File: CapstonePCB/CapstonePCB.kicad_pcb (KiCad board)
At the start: 2 copper layers, 43 parts, among them J1 Conn_02x40_Counter_Clockwise, J2 Barrel_Jack, J3 512964594, SW1 SW_Push, SW2 SW_Push, SW3 SW_Push, U1 NUCLEO64-F411RE, U2 LP-MSPM0G3507, U3 STSPIN220, U4 SN74AHC14N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

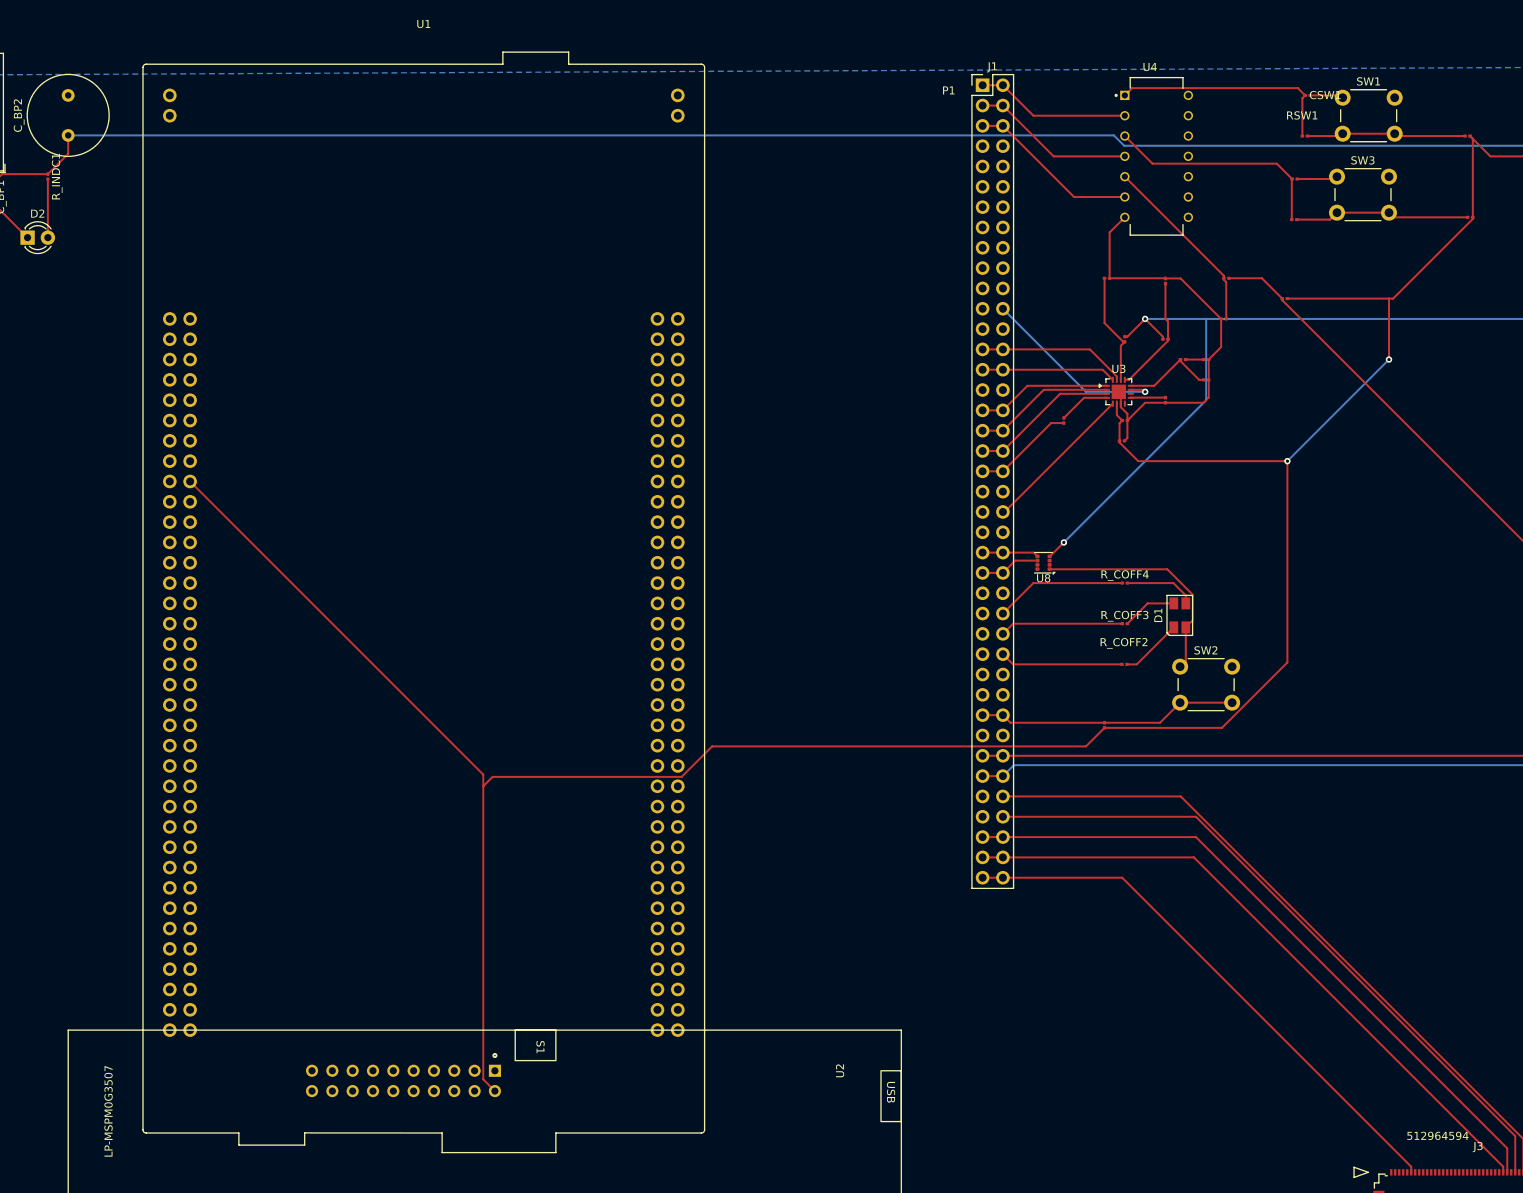
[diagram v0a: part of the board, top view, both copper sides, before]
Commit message: Updated silk-screen
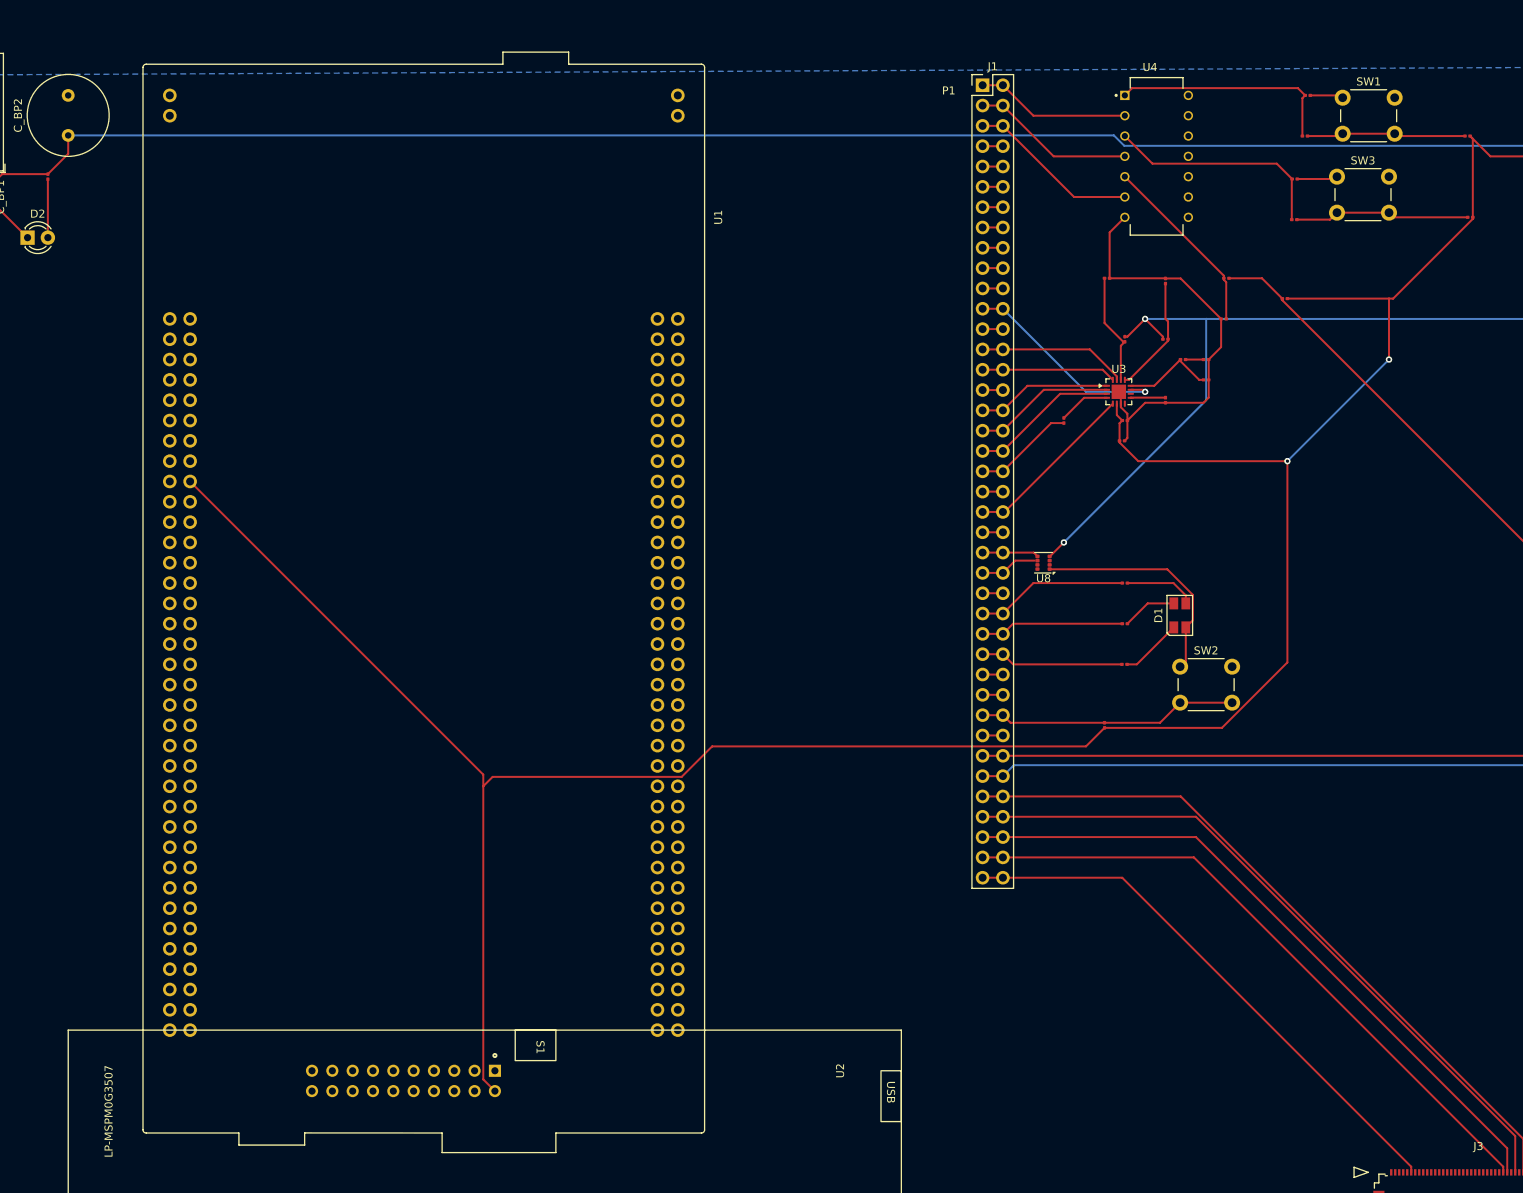
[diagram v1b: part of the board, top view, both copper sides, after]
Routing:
- net Net-(J1-Pin_23): track 24.0 -> 26.5 mm
- net Net-(J1-Pin_57): track 15.4 -> 17.9 mm
- net Net-(J1-Pin_55): track 15.4 -> 18.0 mm
- net Net-(J1-Pin_73): track 85.1 -> 87.7 mm
- net Net-(J1-Pin_71): track 87.0 -> 89.5 mm
- net Net-(J1-Pin_7): track 0.00 -> 2.54 mm
- net Net-(J1-Pin_65): track 0.00 -> 2.54 mm
- net Net-(J1-Pin_61): track 0.00 -> 2.54 mm
- net Net-(J1-Pin_59): track 0.00 -> 2.54 mm
- net Net-(J1-Pin_53): track 16.5 -> 19.0 mm
- net Net-(J1-Pin_51): track 0.00 -> 2.54 mm
- net Net-(J1-Pin_45): track 0.00 -> 2.54 mm
- net Net-(J1-Pin_43): track 19.3 -> 21.9 mm
- net Net-(J1-Pin_41): track 0.00 -> 2.54 mm
- net Net-(J1-Pin_31): track 0.00 -> 2.54 mm
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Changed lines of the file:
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@@
 			(at 0 -1.05 0)
 			(layer "F.SilkS")
+			(hide yes)
 			(effects
 				(font
@@
 			(at -0.345 -2.54 0)
 			(layer "F.SilkS")
+			(hide yes)
 			(effects
 				(font
@@
 			(at 0 -1.05 90)
 			(layer "F.SilkS")
+			(hide yes)
 			(effects
 				(font
@@
 			(layer "F.Fab")
 		)
-		(fp_text user "512964594"
-			(at -5.1816 -6.604 0)
-			(layer "F.SilkS")
-			(effects
-				(font
-					(size 1 1)
-					(thickness 0.15)
-				)
-			)
-		)
-		(fp_text user "512964594"
-			(at -5.1816 -6.604 0)
-			(layer "F.Fab")
-			(effects
-				(font
-					(size 1 1)
-					(thickness 0.15)
-				)
-			)
-		)
 		(pad "1" smd rect
 			(at -11 -2.08)
@@
 			(at -0.055 -2.74 0)
 			(layer "F.SilkS")
+			(hide yes)
 			(effects
 				(font
@@
 			(at 0 -1.05 0)
 			(layer "F.SilkS")
+			(hide yes)
 			(effects
 				(font
@@
 		(tags "ST Morpho Connector 144 STLink")
 		(property "Reference" "U1"
-			(at 31.75 -36.83 0)
+			(at 68.58 -12.7 270)
 			(layer "F.SilkS")
 			(effects
@@
 		)
 		(property "Value" "NUCLEO64-F411RE"
-			(at 31.75 -35.56 0)
+			(at 31.75 -17.78 0)
 			(layer "F.Fab")
 			(effects
@@
 			(at -2.22 0 0)
 			(layer "F.SilkS")
+			(hide yes)
 			(effects
 				(font
@@
 	)
 	(segment
+		(start 147.32 29.21)
+		(end 149.86 29.21)
+		(width 0.25)
+		(layer "F.Cu")
+		(net 118)
+	)
+	(segment
+		(start 147.32 54.61)
+		(end 149.86 54.61)
+		(width 0.25)
+		(layer "F.Cu")
+		(net 119)
+	)
+	(segment
+		(start 147.32 36.83)
+		(end 149.86 36.83)
+		(width 0.25)
+		(layer "F.Cu")
+		(net 120)
+	)
+	(segment
 		(start 152.9325 54.0775)
 		(end 149.86 57.15)
@@
 	)
 	(segment
+		(start 147.32 39.37)
+		(end 149.86 39.37)
+		(width 0.25)
+		(layer "F.Cu")
+		(net 123)
+	)
+	(segment
+		(start 147.32 31.75)
+		(end 149.86 31.75)
+		(width 0.25)
+		(layer "F.Cu")
+		(net 124)
+	)
+	(segment
 		(start 162.8625 54.5775)
 		(end 154.9725 54.5775)
@@
 	)
 	(segment
+		(start 147.32 41.91)
+		(end 149.86 41.91)
+		(width 0.25)
+		(layer "F.Cu")
+		(net 127)
+	)
+	(segment
+		(start 147.32 44.45)
+		(end 149.86 44.45)
+		(width 0.25)
+		(layer "F.Cu")
+		(net 128)
+	)
+	(segment
 		(start 167.3825 54.5775)
 		(end 167.64 54.835)
@@
 	)
 	(segment
+		(start 147.32 46.99)
+		(end 149.86 46.99)
+		(width 0.25)
+		(layer "F.Cu")
+		(net 129)
+	)
+	(segment
 		(start 147.32 21.59)
 		(end 149.86 21.59)
@@
 	)
 	(segment
+		(start 147.32 26.67)
+		(end 149.86 26.67)
+		(width 0.25)
+		(layer "F.Cu")
+		(net 131)
+	)
+	(segment
+		(start 147.32 34.29)
+		(end 149.86 34.29)
+		(width 0.25)
+		(layer "F.Cu")
+		(net 132)
+	)
+	(segment
+		(start 147.32 24.13)
+		(end 149.86 24.13)
+		(width 0.25)
+		(layer "F.Cu")
+		(net 133)
+	)
+	(segment
 		(start 160.0025 55.5775)
 		(end 157.48 58.1)
@@
 	)
 	(segment
-		(start 169.5 96.2)
-		(end 172.01 93.69)
+		(start 147.32 95.25)
+		(end 149.86 95.25)
 		(width 0.25)
 		(layer "F.Cu")
@@
 	)
 	(segment
-		(start 147.32 95.25)
-		(end 149.86 95.25)
+		(start 169.5 96.2)
+		(end 172.01 93.69)
 		(width 0.25)
 		(layer "F.Cu")
@@
 	)
 	(segment
+		(start 147.32 72.39)
+		(end 149.86 72.39)
+		(width 0.25)
+		(layer "F.Cu")
+		(net 149)
+	)
+	(segment
+		(start 147.32 90.17)
+		(end 149.86 90.17)
+		(width 0.25)
+		(layer "F.Cu")
+		(net 150)
+	)
+	(segment
 		(start 147.32 102.87)
 		(end 149.86 102.87)
@@
 	)
 	(segment
+		(start 147.32 105.41)
+		(end 149.86 105.41)
+		(width 0.25)
+		(layer "F.Cu")
+		(net 152)
+	)
+	(segment
 		(start 172.08781 105.41)
 		(end 149.86 105.41)
@@
 	)
 	(segment
+		(start 147.32 87.63)
+		(end 149.86 87.63)
+		(width 0.25)
+		(layer "F.Cu")
+		(net 153)
+	)
+	(segment
 		(start 164.735 88.9)
 		(end 151.13 88.9)
@@
 	)
 	(segment
+		(start 147.32 82.55)
+		(end 149.86 82.55)
+		(width 0.25)
+		(layer "F.Cu")
+		(net 154)
+	)
+	(segment
 		(start 153.67 78.74)
 		(end 149.86 82.55)
@@
 	)
 	(segment
+		(start 147.32 80.01)
+		(end 149.86 80.01)
+		(width 0.25)
+		(layer "F.Cu")
+		(net 155)
+	)
+	(segment
 		(start 151.395 75.935)
 		(end 153.82175 75.935)
@@
 	)
 	(segment
+		(start 147.32 107.95)
+		(end 149.86 107.95)
+		(width 0.25)
+		(layer "F.Cu")
+		(net 160)
+	)
+	(segment
 		(start 213.9 152.4)
 		(end 213.9 147.86)
@@
 	)
 	(segment
+		(start 147.32 92.71)
+		(end 149.86 92.71)
+		(width 0.25)
+		(layer "F.Cu")
+		(net 162)
+	)
+	(segment
+		(start 147.32 97.79)
+		(end 149.86 97.79)
+		(width 0.25)
+		(layer "F.Cu")
+		(net 163)
+	)
+	(segment
 		(start 147.32 74.93)
 		(end 149.86 74.93)
@@
 	)
 	(segment
+		(start 147.32 67.31)
+		(end 149.86 67.31)
+		(width 0.25)
+		(layer "F.Cu")
+		(net 165)
+	)
+	(segment
+		(start 147.32 69.85)
+		(end 149.86 69.85)
+		(width 0.25)
+		(layer "F.Cu")
+		(net 166)
+	)
+	(segment
 		(start 163.6 56.315)
 		(end 150.065 69.85)
@@
 		(width 0.25)
 		(layer "F.Cu")
+		(net 167)
+	)
+	(segment
+		(start 147.32 85.09)
+		(end 149.86 85.09)
+		(width 0.25)
+		(layer "F.Cu")

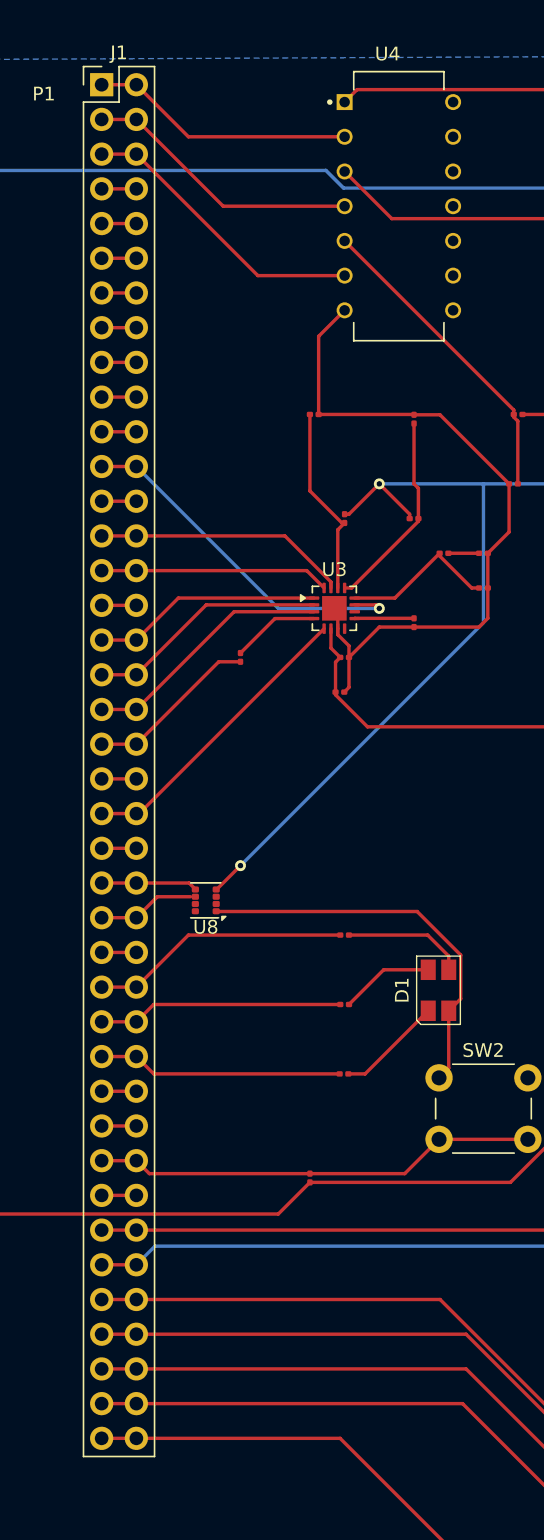
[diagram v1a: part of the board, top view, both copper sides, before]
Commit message: Changed I2C light sensor to different type so pin spacing is not an issue
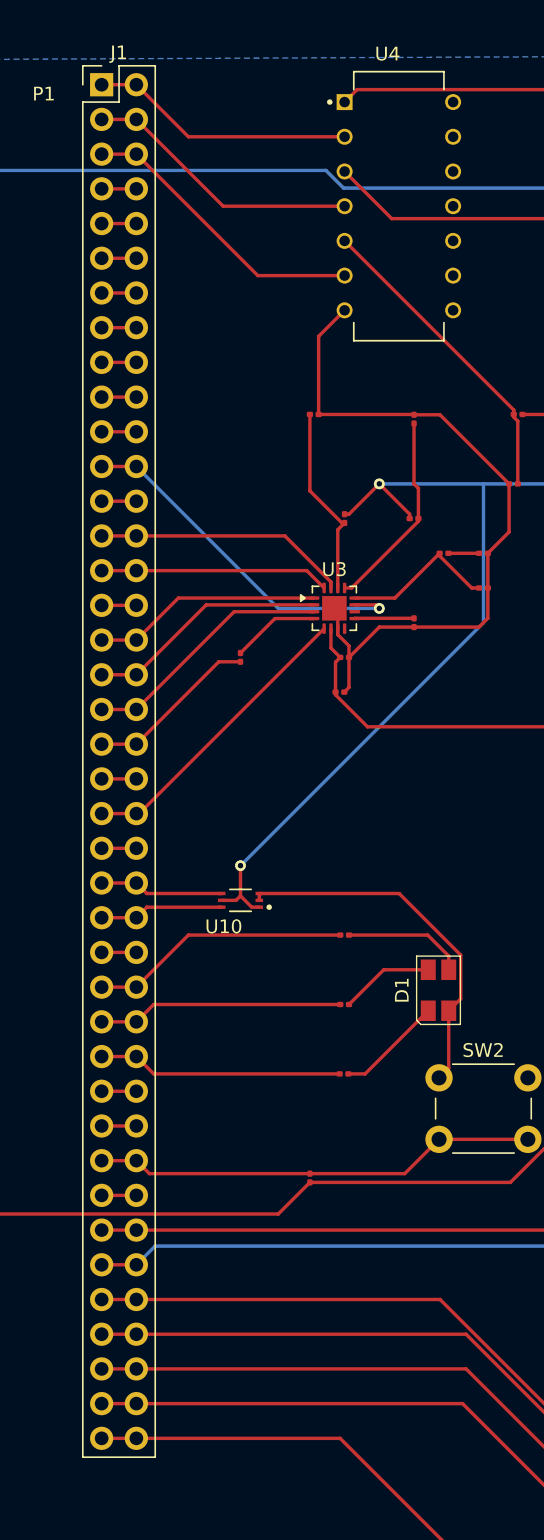
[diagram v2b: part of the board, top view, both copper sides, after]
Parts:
- removed U8: APDS-9306, OptoDevice:Broadcom_LGA-8_2x2mm_P0.53mm
- added U10: BH1750FVI-TR, BH1750FVI-TR:XDCR_BH1750FVI-TR, F.Cu at (157.5, 76.2)
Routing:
- net VDD: track 285.0 -> 287.9 mm
- net GNDREF: track 153.4 -> 151.3 mm
- net Net-(J1-Pin_47): track 7.05 -> 9.10 mm
- net Net-(J1-Pin_49): track 7.14 -> 9.10 mm

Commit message: Added backlight power for LCD
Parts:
- added U9: AL5809-20QP1-7, AL5809-20.step:SODFL3717X100N, F.Cu at (222.2, 160.0)
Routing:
- net +12V: track 261.0 -> 417.7 mm
- net Net-(U9-OUT): track 0.00 -> 8.76 mm
